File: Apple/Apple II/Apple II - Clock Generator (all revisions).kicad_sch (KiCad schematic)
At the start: 31 parts, among them Q1 2N4258, Q2 2N4258, Y1 14.318MHz

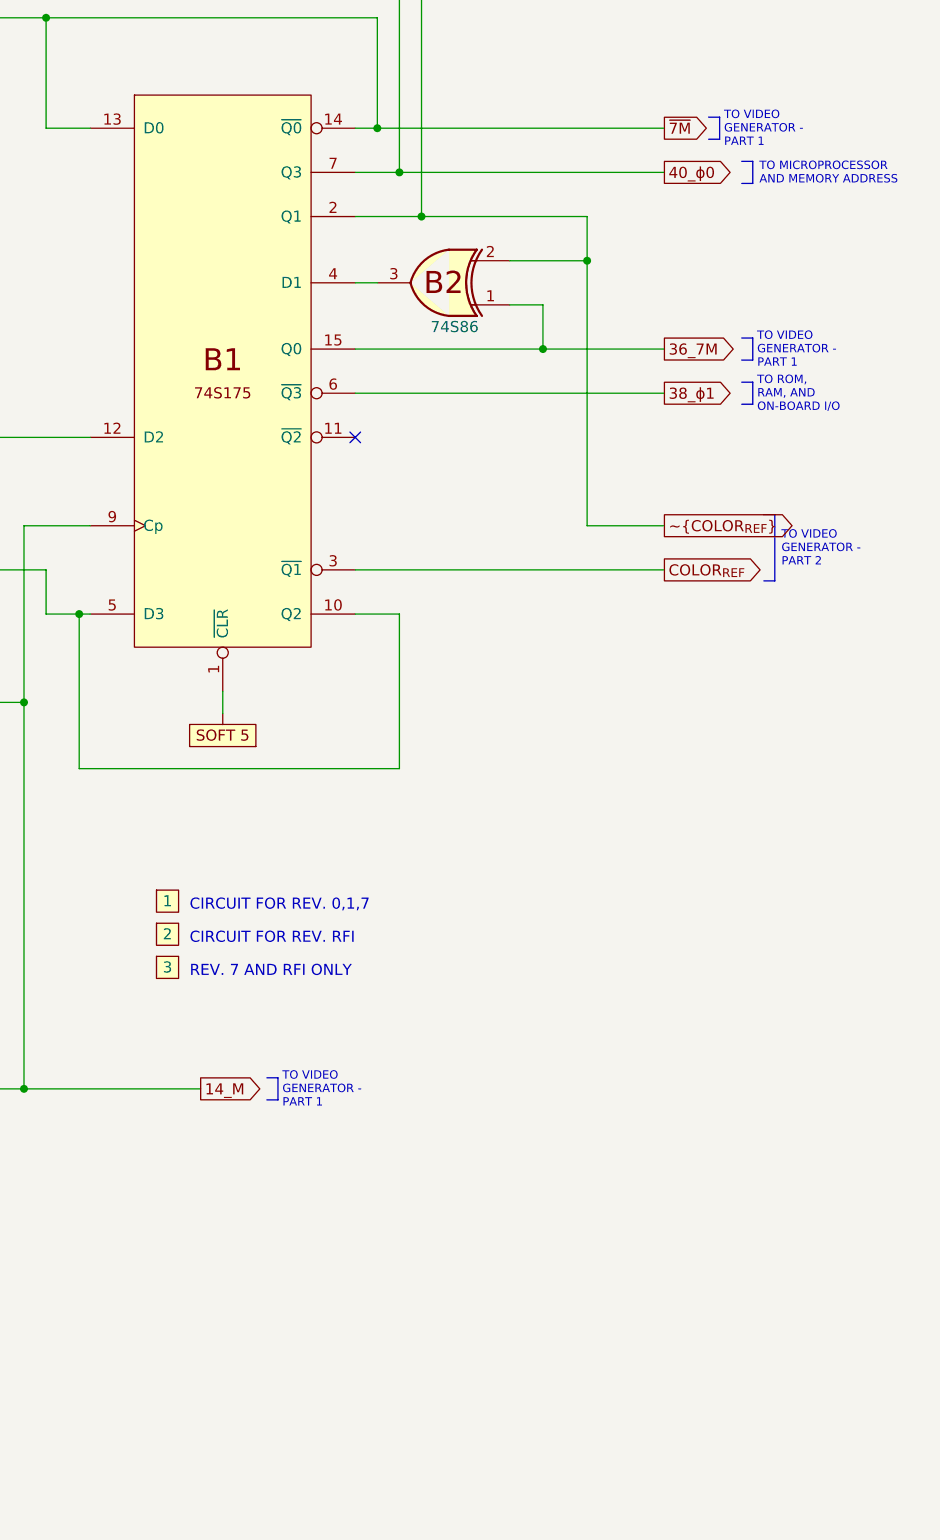
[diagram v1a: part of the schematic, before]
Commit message: Completed Apple II -  Memory Address Pt 1 of 2 (Rev 0,1)
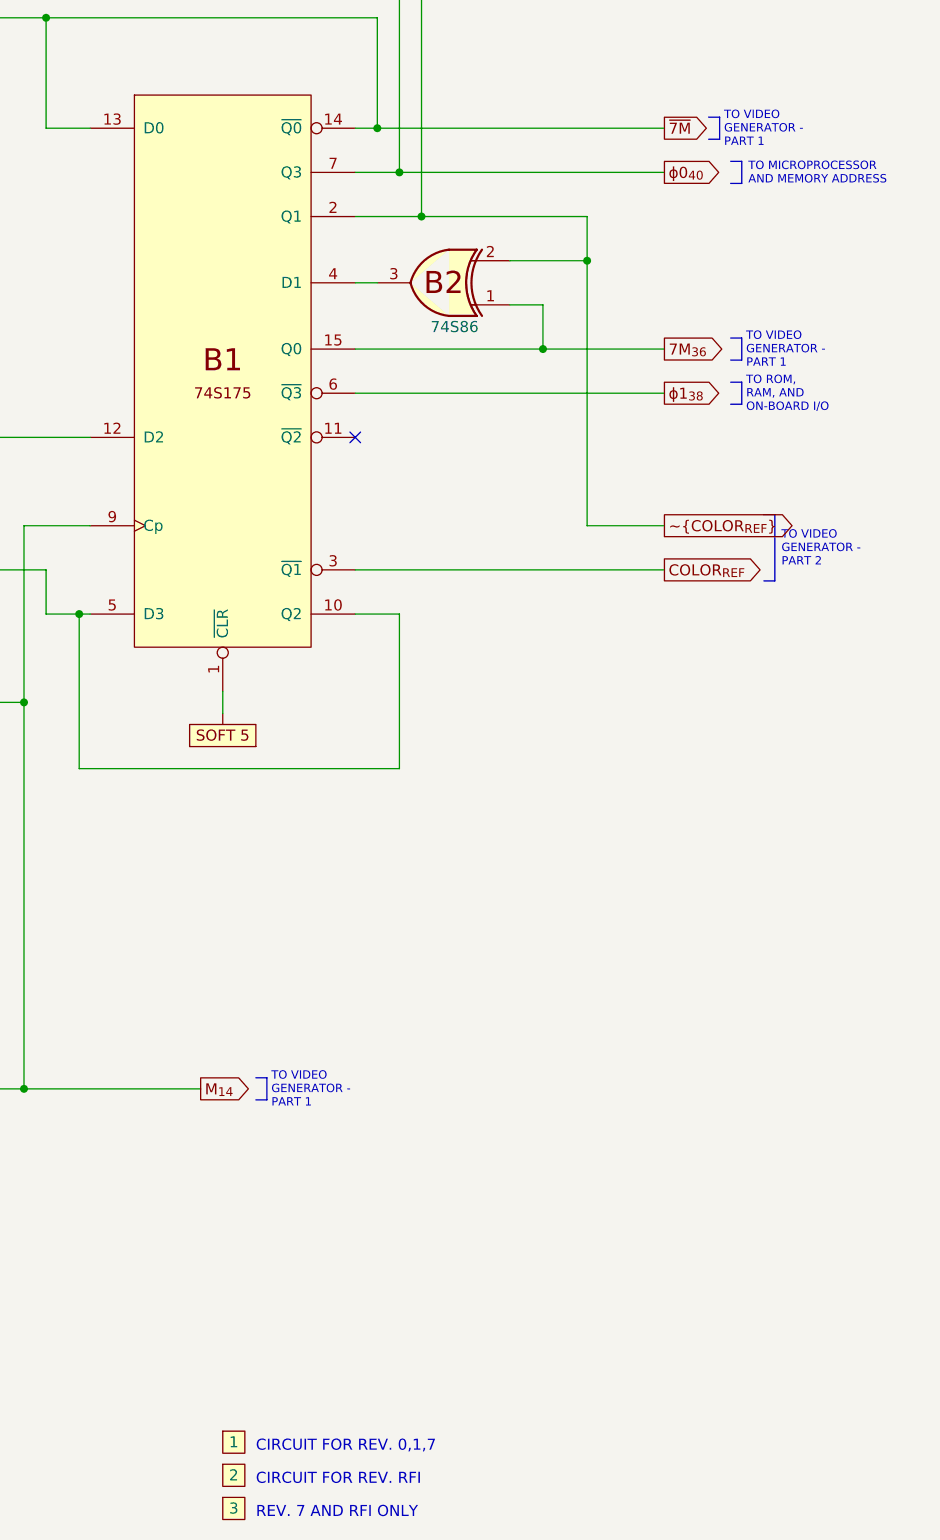
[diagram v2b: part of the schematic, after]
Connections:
- net 14_M renamed M_{14}
- net 36_7M renamed 7M_{36}
- net 38_ɸ1 renamed ɸ1_{38}
- net 40_ɸ0 renamed ɸ0_{40}

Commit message: Finished Apple II - Sheet 6 - Memory Address Pt 2 of 2 (All Revisions)
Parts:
- removed O1, O2, O? (x5): SOFT_5, symbol Apple II:SOFT_5
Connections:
- net ɸ0_{40}: now also D2.4; no longer D2.5
- net SOFT 5: now reaches B1.1 (~{CLR})
- net SOFT 5: now also A2.11, A2.8, B2.4, C2.1 (~{CLR}), R28.1
- net at A2.2, B12.11, B13.10: now also D2.5; no longer D2.4

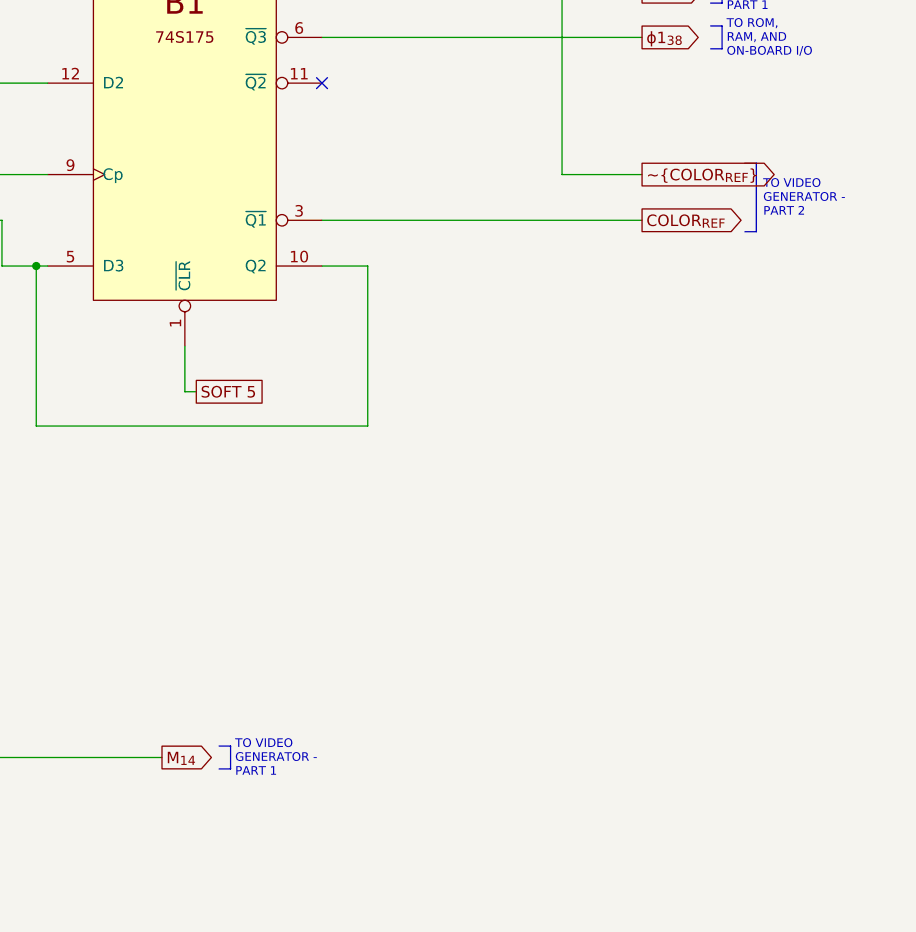
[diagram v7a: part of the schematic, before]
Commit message: Finished Apple II - Sheet 11 - Peripheral I/O (all revisions)
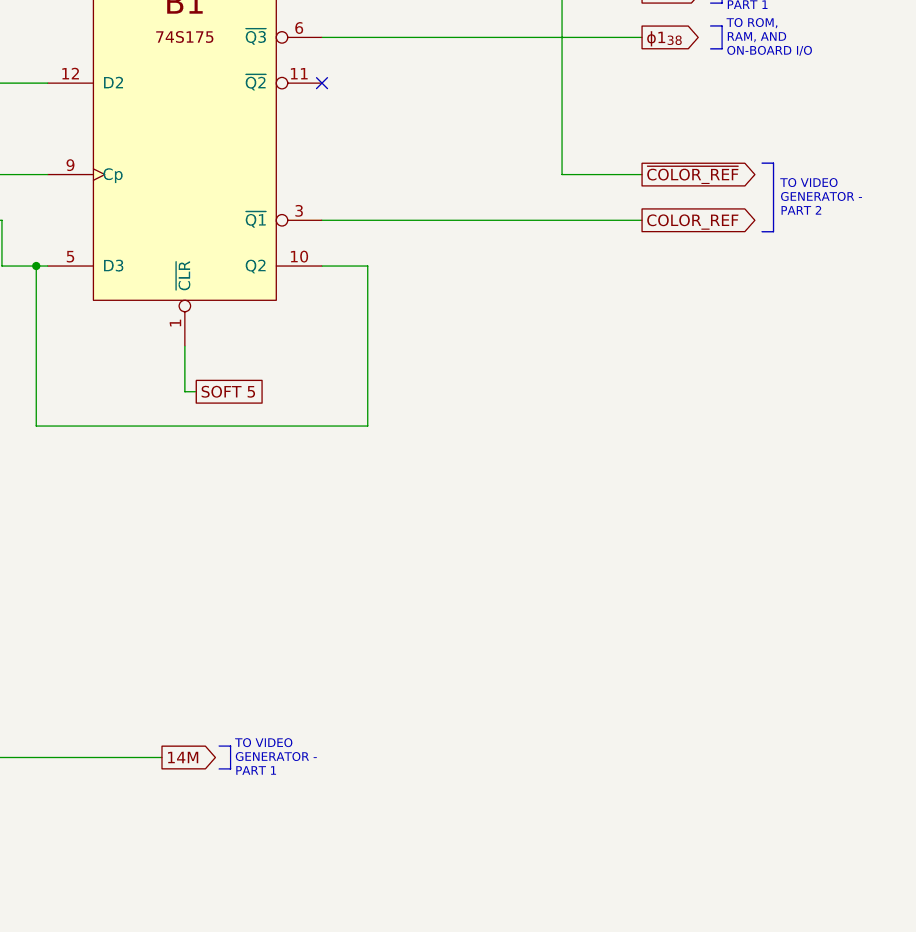
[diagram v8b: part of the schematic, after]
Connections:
- net COLOR_{REF} renamed COLOR_REF
- net M_{14} renamed 14M
- net ~{COLOR_{REF}} renamed ~{COLOR_REF}
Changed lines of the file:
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@@
     (stroke (width 0) (type default) (color 0 0 0 0))
   )
-  (polyline (pts (xy 363.22 143.51) (xy 364.49 143.51))
+  (polyline (pts (xy 365.125 143.51) (xy 366.395 143.51))
     (stroke (width 0) (type solid) (color 0 0 0 0))
   )
@@
     (stroke (width 0) (type default) (color 0 0 0 0))
   )
-  (polyline (pts (xy 364.49 135.89) (xy 364.49 143.51))
+  (polyline (pts (xy 366.395 135.89) (xy 366.395 143.51))
     (stroke (width 0) (type solid) (color 0 0 0 0))
   )
@@
     (stroke (width 0) (type solid) (color 0 0 0 0))
   )
-  (polyline (pts (xy 363.22 135.89) (xy 364.49 135.89))
+  (polyline (pts (xy 365.125 135.89) (xy 366.395 135.89))
     (stroke (width 0) (type solid) (color 0 0 0 0))
   )
@@
     (effects (font (size 0.96 0.96)) (justify left bottom))
   )
-  (text "TO VIDEO\nGENERATOR -\nPART 2" (at 365.252 141.986 0)
+  (text "TO VIDEO\nGENERATOR -\nPART 2" (at 367.157 141.986 0)
     (effects (font (size 0.96 0.96)) (justify left bottom))
   )
@@
     )
   )
-  (global_label "M_{14}" (shape output) (at 298.45 201.93 0) (fields_autoplaced)
-    (effects (font (size 1.27 1.27)) (justify left))
-    (property "Intersheet References" "${INTERSHEET_REFS}" (id 0) (at 304.2498 201.8506 0)
+  (global_label "14M" (shape output) (at 298.45 201.93 0) (fields_autoplaced)
+    (effects (font (size 1.27 1.27)) (justify left))
+    (property "Intersheet References" "${INTERSHEET_REFS}" (id 0) (at 304.7336 201.8506 0)
       (effects (font (size 1.27 1.27)) (justify left) hide)
     )
@@
     )
   )
-  (global_label "COLOR_{REF}" (shape output) (at 351.79 142.24 0) (fields_autoplaced)
-    (effects (font (size 1.27 1.27)) (justify left))
-    (property "Intersheet References" "${INTERSHEET_REFS}" (id 0) (at 363.2382 142.1606 0)
+  (global_label "COLOR_REF" (shape output) (at 351.79 142.24 0) (fields_autoplaced)
+    (effects (font (size 1.27 1.27)) (justify left))
+    (property "Intersheet References" "${INTERSHEET_REFS}" (id 0) (at 364.9074 142.1606 0)
       (effects (font (size 1.27 1.27)) (justify left) hide)
     )
@@
     )
   )
-  (global_label "~{COLOR_{REF}}" (shape output) (at 351.79 137.16 0) (fields_autoplaced)
-    (effects (font (size 1.27 1.27)) (justify left))
-    (property "Intersheet References" "${INTERSHEET_REFS}" (id 0) (at 363.2382 137.0806 0)
-      (effects (font (size 1.27 1.27)) (justify left) hide)
-    )
+  (global_label "~{COLOR_REF}" (shape output) (at 351.79 137.16 0) (fields_autoplaced)
+    (effects (font (size 1.27 1.27)) (justify left))
+    (property "Intersheet References" "${INTERSHEET_REFS}" (id 0) (at 364.9074 137.0806 0)
+      (effects (font (size 1.27 1.27)) (justify left) hide)
+    )
